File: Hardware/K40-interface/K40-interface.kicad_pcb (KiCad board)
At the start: 2 copper layers, 14 parts, among them P1 CONN_01X08, P2 CONN_01X04, P3 CONN_01X04, P4 CONN_01X04, P5 CONN_01X04, U1 4049, U2 4N25

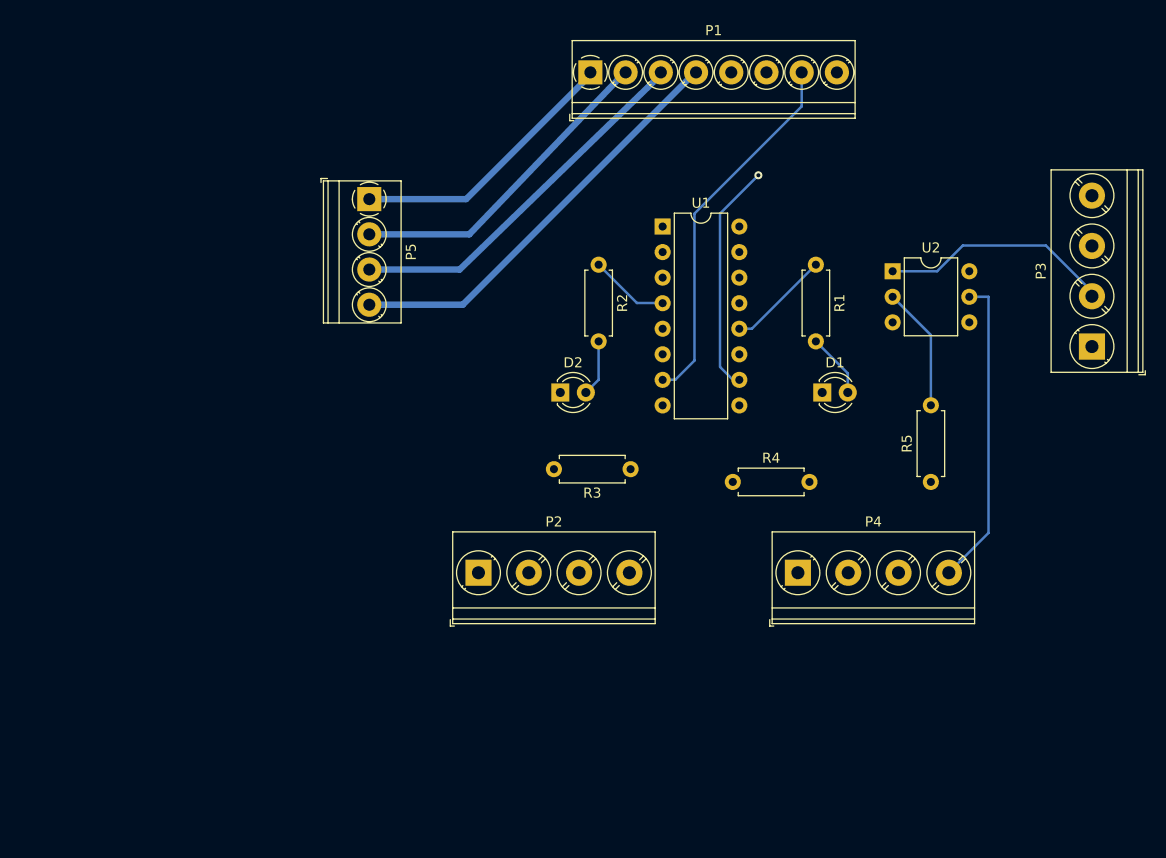
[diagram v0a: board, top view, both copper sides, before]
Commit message: Added PDF of schematic
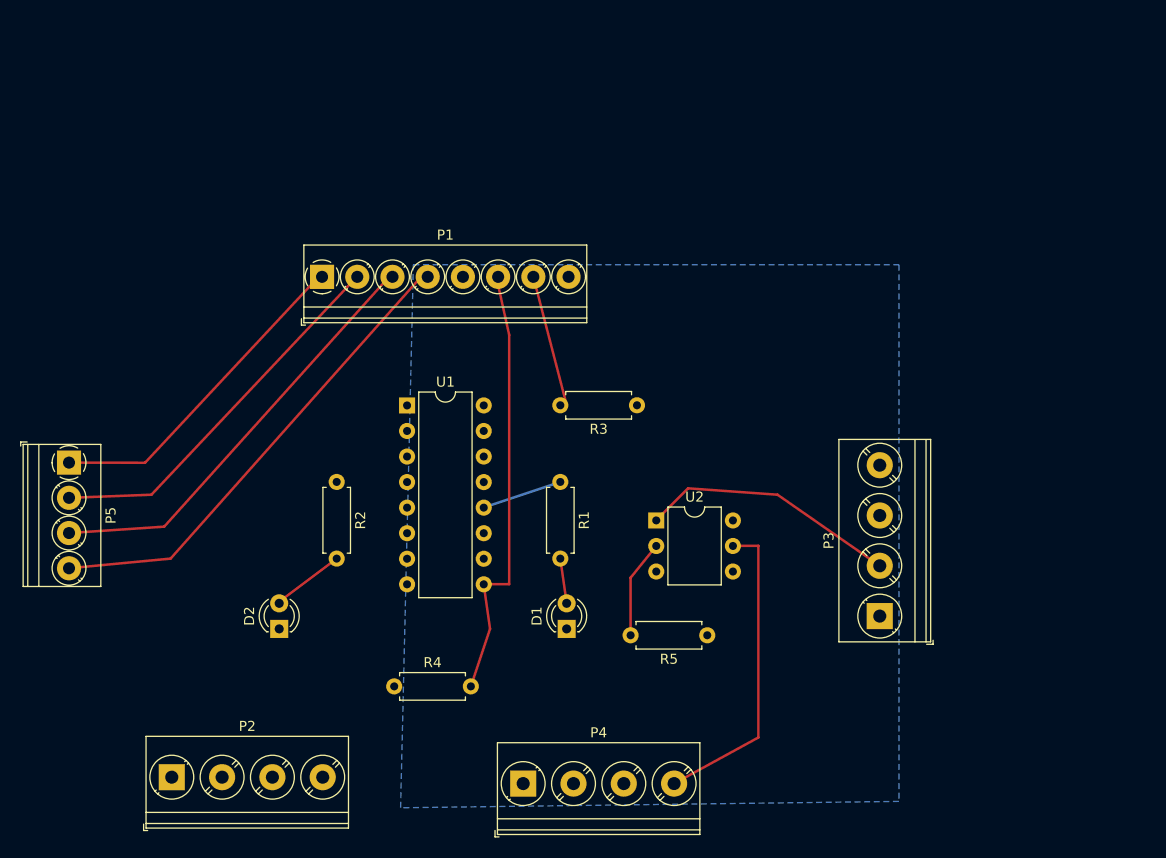
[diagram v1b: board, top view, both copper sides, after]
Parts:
- moved P5 39.7 mm to (86.4, 93.3)
- moved R4 39.3 mm to (118.7, 115.6)
- moved P2 36.6 mm to (96.6, 124.6)
- moved D2 36.5 mm to (107.3, 109.9), turned to 90 degrees
- moved D1 34.6 mm to (135.9, 109.9), turned to 90 degrees
- moved P4 34.4 mm to (131.6, 125.2)
- moved U2 34.1 mm to (144.8, 99.1)
- moved P3 34.1 mm to (167.0, 108.6)
- moved R2 33.8 mm to (113.0, 95.2)
- moved P1 33.5 mm to (111.6, 74.9)
- moved R1 33.3 mm to (135.3, 95.2)
- moved U1 31.0 mm to (120.0, 87.6)
- moved R5 26.9 mm to (149.9, 110.5), turned to 180 degrees
- moved R3 6.38 mm to (142.9, 87.6)
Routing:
- net Net-(P1-Pad6): track 0.00 -> 43.7 mm
- net Net-(P1-Pad7): track 37.0 -> 13.2 mm
- net Net-(U1-Pad10): track 23.1 -> 0.00 mm, vias 1 -> 0
- net Net-(R2-Pad1): track 7.93 -> 0.00 mm
- net Net-(P1-Pad4): track 41.9 -> 49.0 mm
- net Net-(P1-Pad3): track 37.1 -> 43.7 mm
- net Net-(P1-Pad2): track 32.2 -> 38.7 mm
- net Net-(P1-Pad1): track 28.0 -> 33.6 mm
- net Net-(R5-Pad2): track 12.4 -> 9.14 mm
- net Net-(P3-Pad2): track 23.5 -> 25.8 mm
- net Net-(R1-Pad1): track 10.2 -> 8.03 mm
- net Net-(D1-Pad2): track 6.40 -> 4.49 mm
- net Net-(D2-Pad2): track 5.61 -> 6.35 mm
- added copper zone on B.Cu, net +5V

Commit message: Changes to interface PCB layout - test
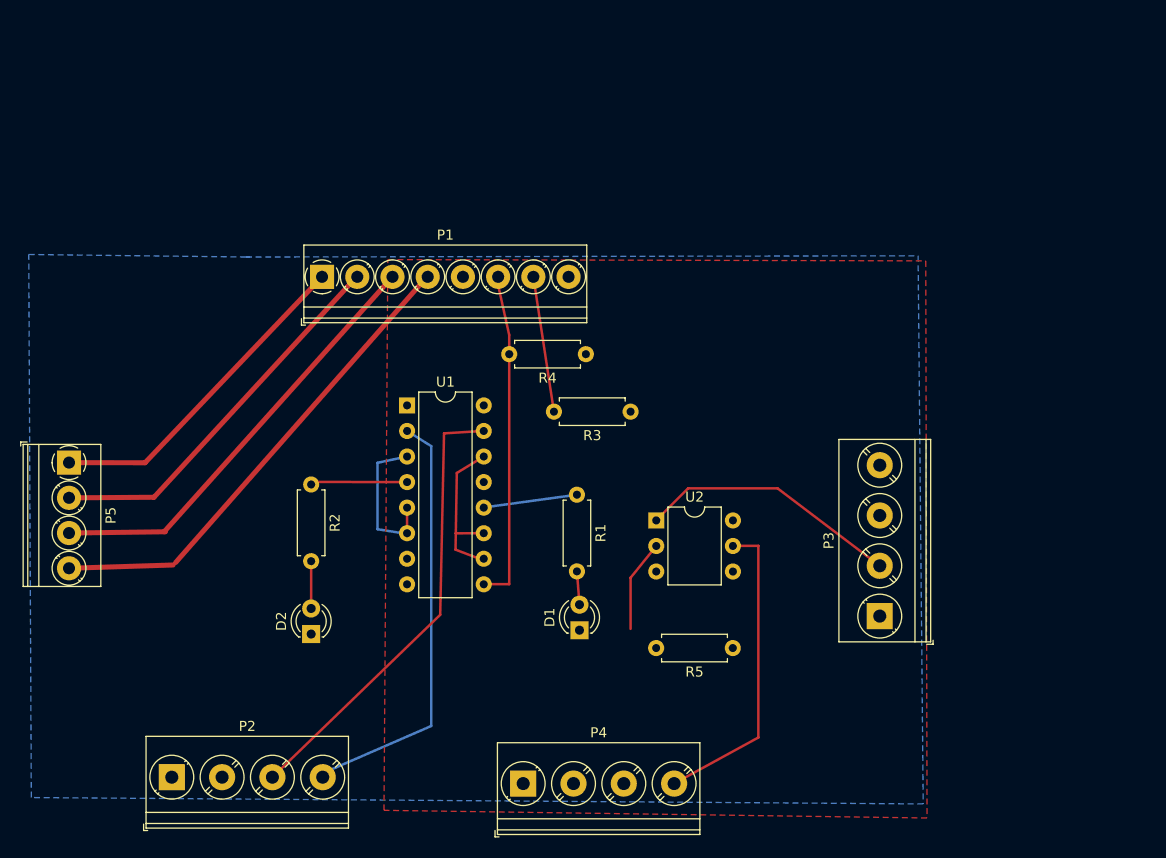
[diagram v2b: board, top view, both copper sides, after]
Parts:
- moved R4 38.1 mm to (137.8, 82.5), turned to 180 degrees
- moved D2 3.22 mm to (110.5, 110.4)
- moved R5 2.84 mm to (152.4, 111.8)
- moved R2 2.55 mm to (110.5, 95.5)
- moved R1 2.08 mm to (136.9, 96.5)
- moved D1 1.28 mm to (137.2, 110.0)
- moved R3 0.90 mm to (142.2, 88.3)
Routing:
- net Net-(P2-Pad3): track 0.00 -> 45.3 mm
- net Net-(P2-Pad4): track 0.00 -> 42.4 mm
- net Net-(U1-Pad10): track 0.00 -> 16.4 mm
- net Net-(U1-Pad3): track 0.00 -> 15.5 mm
- net Net-(P1-Pad6): track 43.7 -> 33.2 mm
- net Net-(R2-Pad1): track 0.00 -> 9.54 mm
- net Net-(D2-Pad2): track 6.35 -> 4.32 mm
- net Net-(R1-Pad1): track 8.03 -> 9.36 mm
- net Net-(D1-Pad2): track 4.49 -> 3.31 mm
- net Net-(P1-Pad4): track 49.0 -> 48.2 mm
- added copper zone on F.Cu, net +5V
- added copper zone on B.Cu, net GND
- removed copper zone on B.Cu, net +5V
